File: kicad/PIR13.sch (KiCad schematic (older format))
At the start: 22 parts, among them P301 PIR13, Q301 IRLML2502, Q302 IRLML2502, Q303 IRLML2502

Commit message: Started assigning foot prints to the parts
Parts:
- C301, C302, C303: footprint (none) -> Capacitors_SMD:C_0805
- D301, D302, D303: footprint (none) -> LEDs:LED_0805
- P301: footprint (none) -> Pin_Headers:Pin_Header_Straight_1x09; Conrad-PN (none) -> Value; Digikey-PN (none) -> Value; MFP (none) -> Value
- Q301, Q302, Q303: footprint Micro3 -> TO_SOT_Packages_SMD:SOT-23; Conrad-PN (none) -> 162827 - 62; Digikey-PN (none) -> IRLML2502GTRPBFCT-ND; MFP TPS70933DBVR -> IRLML2502GTRPBF
- R301, R302, R303: footprint (none) -> Resistors_SMD:R_0805
- R304: renamed from R307; footprint (none) -> Resistors_SMD:R_0805
- R305: renamed from R308; footprint (none) -> Resistors_SMD:R_0805
- R306: renamed from R309; footprint (none) -> Resistors_SMD:R_0805
- R307: renamed from R304; footprint (none) -> Resistors_SMD:R_0805
- R308: renamed from R305; footprint (none) -> Resistors_SMD:R_0805
- R309: renamed from R306; footprint (none) -> Resistors_SMD:R_0805
- TP301, TP302: footprint (none) -> Measurement_Points:Measurement_Point_Round-SMD-Pad_Small
- TP303: renamed from TP?; footprint (none) -> Measurement_Points:Measurement_Point_Round-SMD-Pad_Small

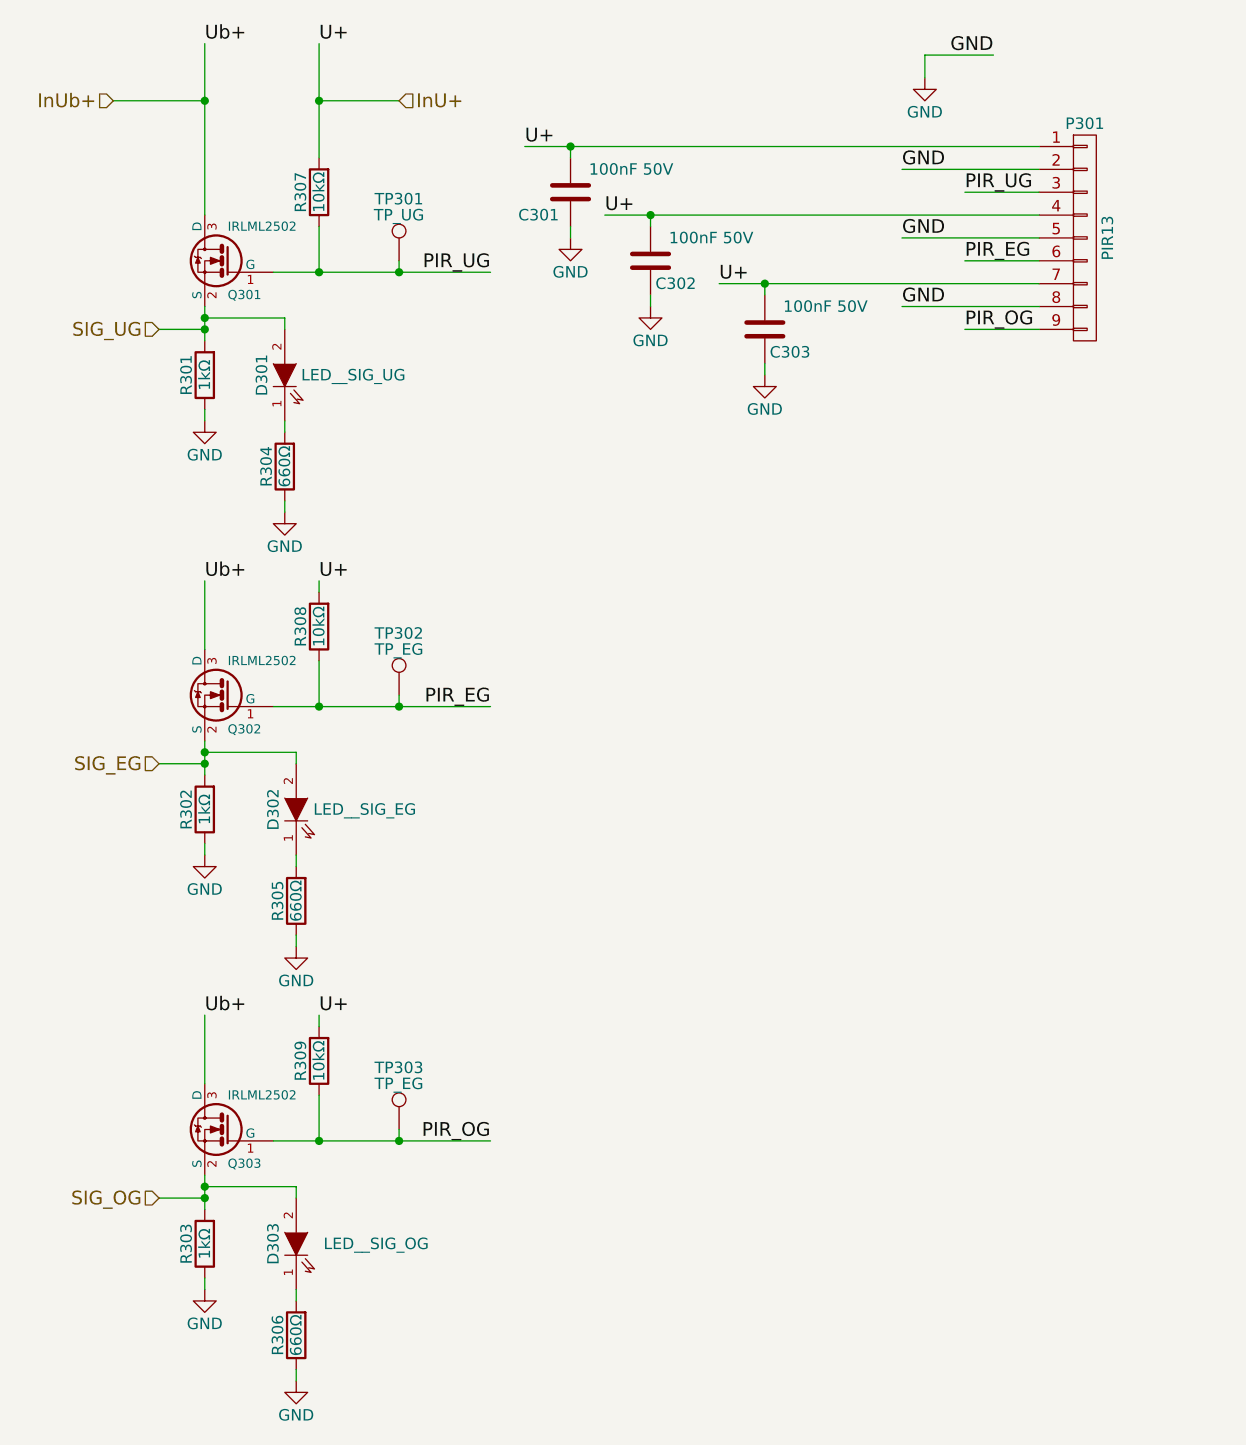
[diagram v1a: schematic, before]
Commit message: Started adding tracks to the layout
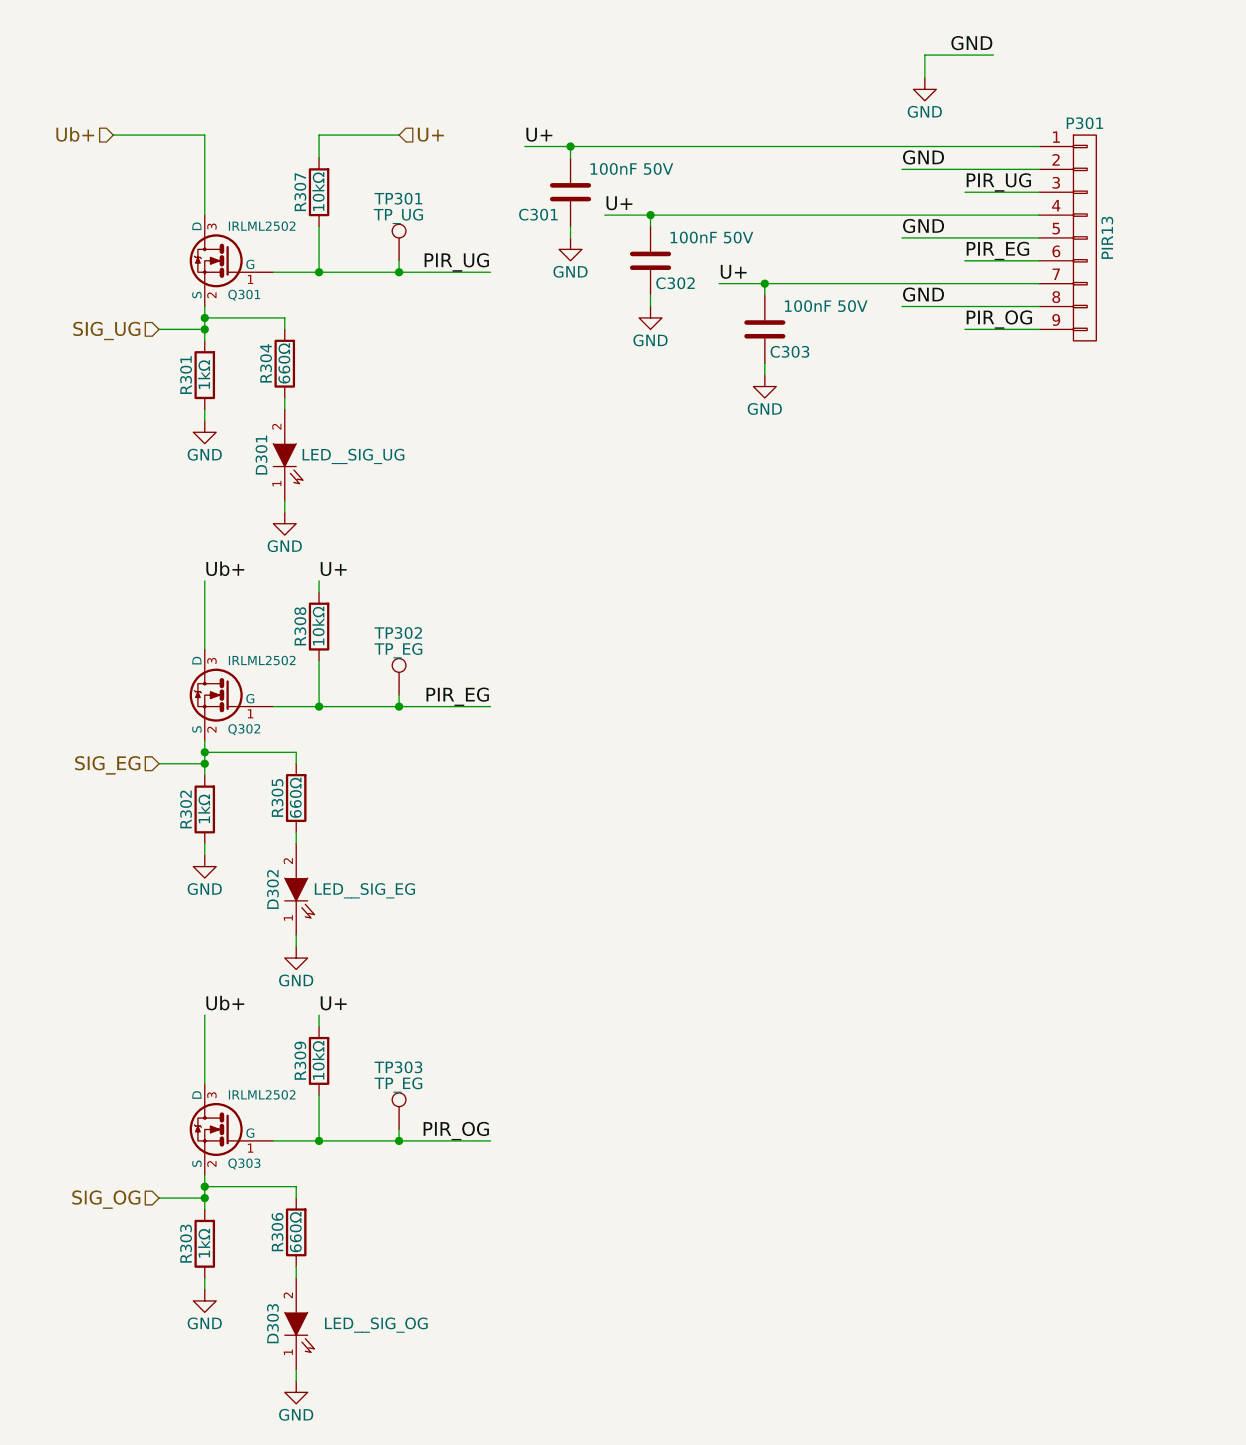
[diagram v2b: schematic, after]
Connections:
- net GND: now also D301.1 (K), D302.1 (K), D303.1 (K); no longer R304.1, R305.1, R306.1
- net SIG_EG: now also R305.2; no longer D302.2 (A)
- net SIG_OG: now also R306.2; no longer D303.2 (A)
- net SIG_UG: now also R304.2; no longer D301.2 (A)
- net InU+ renamed U+
- net InUb+ renamed Ub+
- new net: D301.2 (A), R304.1
- new net: D302.2 (A), R305.1
- new net: D303.2 (A), R306.1
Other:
- moved on the sheet: D301, D302, D303, R304, R305, R306
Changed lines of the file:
@@
 PIR_OG
 $Comp
-L GND #PWR015
+L GND #PWR018
 U 1 1 585206AF
 P 5550 1150
-F 0 "#PWR015" H 5550 900 50  0001 C CNN
+F 0 "#PWR018" H 5550 900 50  0001 C CNN
 F 1 "GND" H 5550 1000 50  0000 C CNN
 F 2 "" H 5550 1150 50  0000 C CNN
@@
 	-1   0    0    1
 $EndComp
-Text HLabel 3250 1250 2    60   Input ~ 0
-InU+
+Text HLabel 3250 1400 2    60   Input ~ 0
+U+
 Text Label 5450 1550 0    60   ~ 0
 GND
@@
 	-1   0    0    -1
 $EndComp
-Text Label 2400 1000 0    60   ~ 0
-Ub+
 $Comp
 L R R301
@@
 	-1   0    0    1
 $EndComp
-Text Label 2900 1000 0    60   ~ 0
-U+
 Text Label 3650 2000 2    60   ~ 0
 PIR_UG
-Text HLabel 2000 1250 0    60   Input ~ 0
-InUb+
-$Comp
-L GND #PWR016
+Text HLabel 2000 1400 0    60   Input ~ 0
+Ub+
+$Comp
+L GND #PWR019
 U 1 1 585215A4
 P 2400 2650
-F 0 "#PWR016" H 2400 2400 50  0001 C CNN
+F 0 "#PWR019" H 2400 2400 50  0001 C CNN
 F 1 "GND" H 2400 2500 50  0000 C CNN
 F 2 "" H 2400 2650 50  0000 C CNN
@@
 PIR_EG
 $Comp
-L GND #PWR017
+L GND #PWR020
 U 1 1 58521B24
 P 2400 4550
-F 0 "#PWR017" H 2400 4300 50  0001 C CNN
+F 0 "#PWR020" H 2400 4300 50  0001 C CNN
 F 1 "GND" H 2400 4400 50  0000 C CNN
 F 2 "" H 2400 4550 50  0000 C CNN
@@
 PIR_OG
 $Comp
-L GND #PWR018
+L GND #PWR021
 U 1 1 58521C75
 P 2400 6450
-F 0 "#PWR018" H 2400 6200 50  0001 C CNN
+F 0 "#PWR021" H 2400 6200 50  0001 C CNN
 F 1 "GND" H 2400 6300 50  0000 C CNN
 F 2 "" H 2400 6450 50  0000 C CNN
@@
 L LED D301
 U 1 1 5852C267
-P 2750 2450
-F 0 "D301" H 2750 2550 50  0000 C CNN
-F 1 "LED__SIG_UG" V 2750 2150 50  0000 C CNN
-F 2 "LEDs:LED_0805" H 2750 2450 50  0001 C CNN
-F 3 "" H 2750 2450 50  0000 C CNN
-	1    2750 2450
+P 2750 2800
+F 0 "D301" H 2750 2900 50  0000 C CNN
+F 1 "LED__SIG_UG" V 2750 2500 50  0000 C CNN
+F 2 "LEDs:LED_0805" H 2750 2800 50  0001 C CNN
+F 3 "" H 2750 2800 50  0000 C CNN
+	1    2750 2800
 	0    -1   -1   0
 $EndComp
@@
 L R R304
 U 1 1 5852C57E
-P 2750 2850
-F 0 "R304" V 2830 2850 50  0000 C CNN
-F 1 "660Ω" V 2750 2850 50  0000 C CNN
-F 2 "Resistors_SMD:R_0805" V 2680 2850 50  0001 C CNN
-F 3 "" H 2750 2850 50  0000 C CNN
-	1    2750 2850
+P 2750 2400
+F 0 "R304" V 2830 2400 50  0000 C CNN
+F 1 "660Ω" V 2750 2400 50  0000 C CNN
+F 2 "Resistors_SMD:R_0805" V 2680 2400 50  0001 C CNN
+F 3 "" H 2750 2400 50  0000 C CNN
+	1    2750 2400
 	-1   0    0    1
 $EndComp
@@
 L LED D302
 U 1 1 5852CAA2
-P 2800 4350
-F 0 "D302" H 2800 4450 50  0000 C CNN
-F 1 "LED__SIG_EG" V 2800 4050 50  0000 C CNN
-F 2 "LEDs:LED_0805" H 2800 4350 50  0001 C CNN
-F 3 "" H 2800 4350 50  0000 C CNN
-	1    2800 4350
+P 2800 4700
+F 0 "D302" H 2800 4800 50  0000 C CNN
+F 1 "LED__SIG_EG" V 2800 4400 50  0000 C CNN
+F 2 "LEDs:LED_0805" H 2800 4700 50  0001 C CNN
+F 3 "" H 2800 4700 50  0000 C CNN
+	1    2800 4700
 	0    -1   -1   0
 $EndComp
@@
 L R R305
 U 1 1 5852CAA8
-P 2800 4750
-F 0 "R305" V 2880 4750 50  0000 C CNN
-F 1 "660Ω" V 2800 4750 50  0000 C CNN
-F 2 "Resistors_SMD:R_0805" V 2730 4750 50  0001 C CNN
-F 3 "" H 2800 4750 50  0000 C CNN
-	1    2800 4750
-	-1   0    0    1
-$EndComp
-$Comp
-L GND #PWR019
+P 2800 4300
+F 0 "R305" V 2880 4300 50  0000 C CNN
+F 1 "660Ω" V 2800 4300 50  0000 C CNN
+F 2 "Resistors_SMD:R_0805" V 2730 4300 50  0001 C CNN
+F 3 "" H 2800 4300 50  0000 C CNN
+	1    2800 4300
+	-1   0    0    1
+$EndComp
+$Comp
+L GND #PWR022
 U 1 1 5852CAAF
 P 2800 4950
-F 0 "#PWR019" H 2800 4700 50  0001 C CNN
+F 0 "#PWR022" H 2800 4700 50  0001 C CNN
 F 1 "GND" H 2800 4800 50  0000 C CNN
 F 2 "" H 2800 4950 50  0000 C CNN
@@
 L LED D303
 U 1 1 5852D26A
-P 2800 6250
-F 0 "D303" H 2800 6350 50  0000 C CNN
-F 1 "LED__SIG_OG" V 2800 5900 50  0000 C CNN
-F 2 "LEDs:LED_0805" H 2800 6250 50  0001 C CNN
-F 3 "" H 2800 6250 50  0000 C CNN
-	1    2800 6250
+P 2800 6600
+F 0 "D303" H 2800 6700 50  0000 C CNN
+F 1 "LED__SIG_OG" V 2800 6250 50  0000 C CNN
+F 2 "LEDs:LED_0805" H 2800 6600 50  0001 C CNN
+F 3 "" H 2800 6600 50  0000 C CNN
+	1    2800 6600
 	0    -1   -1   0
 $EndComp
@@
 L R R306
 U 1 1 5852D270
-P 2800 6650
-F 0 "R306" V 2880 6650 50  0000 C CNN
-F 1 "660Ω" V 2800 6650 50  0000 C CNN
-F 2 "Resistors_SMD:R_0805" V 2730 6650 50  0001 C CNN
-F 3 "" H 2800 6650 50  0000 C CNN
-	1    2800 6650
-	-1   0    0    1
-$EndComp
-$Comp
-L GND #PWR020
+P 2800 6200
+F 0 "R306" V 2880 6200 50  0000 C CNN
+F 1 "660Ω" V 2800 6200 50  0000 C CNN
+F 2 "Resistors_SMD:R_0805" V 2730 6200 50  0001 C CNN
+F 3 "" H 2800 6200 50  0000 C CNN
+	1    2800 6200
+	-1   0    0    1
+$EndComp
+$Comp
+L GND #PWR023
 U 1 1 5852D277
 P 2800 6850
-F 0 "#PWR020" H 2800 6600 50  0001 C CNN
+F 0 "#PWR023" H 2800 6600 50  0001 C CNN
 F 1 "GND" H 2800 6700 50  0000 C CNN
 F 2 "" H 2800 6850 50  0000 C CNN
@@
 $EndComp
 $Comp
-L GND #PWR021
+L GND #PWR024
 U 1 1 5852E037
 P 4000 1850
-F 0 "#PWR021" H 4000 1600 50  0001 C CNN
+F 0 "#PWR024" H 4000 1600 50  0001 C CNN
 F 1 "GND" H 4000 1700 50  0000 C CNN
 F 2 "" H 4000 1850 50  0000 C CNN
@@
 $EndComp
 $Comp
-L GND #PWR022
+L GND #PWR025
 U 1 1 5852E38D
 P 4350 2150
-F 0 "#PWR022" H 4350 1900 50  0001 C CNN
+F 0 "#PWR025" H 4350 1900 50  0001 C CNN
 F 1 "GND" H 4350 2000 50  0000 C CNN
 F 2 "" H 4350 2150 50  0000 C CNN
@@
 $EndComp
 $Comp
-L GND #PWR023
+L GND #PWR026
 U 1 1 5852E6E2
 P 4850 2450
-F 0 "#PWR023" H 4850 2200 50  0001 C CNN
+F 0 "#PWR026" H 4850 2200 50  0001 C CNN
 F 1 "GND" H 4850 2300 50  0000 C CNN
 F 2 "" H 4850 2450 50  0000 C CNN
@@
 Connection ~ 2900 2000
 Wire Wire Line
-	2400 1000 2400 1750
-Wire Wire Line
 	2400 2600 2400 2650
 Wire Wire Line
-	2900 1000 2900 1500
-Wire Wire Line
-	2000 1250 2400 1250
-Connection ~ 2400 1250
+	2000 1400 2400 1400
 Wire Wire Line
 	2400 2250 2200 2250
@@
 Connection ~ 2400 6050
 Wire Wire Line
-	2750 2650 2750 2700
-Wire Wire Line
 	2750 3000 2750 3050
-Wire Wire Line
-	2800 4550 2800 4600
 Wire Wire Line
 	2800 4900 2800 4950
@@
 Connection ~ 2400 4100
 Wire Wire Line
-	2800 6450 2800 6500
-Wire Wire Line
 	2800 6800 2800 6850
 Wire Wire Line
@@
 	4850 2400 4850 2450
 Wire Wire Line
-	3250 1250 2900 1250
-Connection ~ 2900 1250
+	3250 1400 2900 1400
 Wire Wire Line
 	4850 2050 4850 2100
@@
 Connection ~ 2400 2200
 $Comp
-L GND #PWR024
+L GND #PWR027
 U 1 1 5852C6FF
 P 2750 3050
-F 0 "#PWR024" H 2750 2800 50  0001 C CNN
+F 0 "#PWR027" H 2750 2800 50  0001 C CNN
 F 1 "GND" H 2750 2900 50  0000 C CNN
 F 2 "" H 2750 3050 50  0000 C CNN
@@
 	1    0    0    -1
 $EndComp
+Wire Wire Line
+	2400 1400 2400 1750
+Wire Wire Line
+	2900 1400 2900 1500
+Wire Wire Line
+	2750 2550 2750 2600
+Wire Wire Line
+	2800 4450 2800 4500
+Wire Wire Line
+	2800 6350 2800 6400
 $EndSCHEMATC

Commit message: Revamped the master pcb layout for the mounting holes and the actual footprint for the terminal blocks
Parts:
- P301: footprint Pin_Headers:Pin_Header_Straight_1x09 -> tl2c-footprint:Spring_Terminal_Block_1_x_9; Reichelt-PN (none) -> AST 041
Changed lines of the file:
@@
 F 0 "P301" H 6250 2350 50  0000 C CNN
 F 1 "PIR13" V 6350 1850 50  0000 C CNN
-F 2 "Pin_Headers:Pin_Header_Straight_1x09" H 6250 1850 50  0001 C CNN
+F 2 "tl2c-footprint:Spring_Terminal_Block_1_x_9" H 6250 1850 50  0001 C CNN
 F 3 "" H 6250 1850 50  0000 C CNN
 F 4 "Value" H 6250 1850 60  0001 C CNN "MFP"
 F 5 "Value" H 6250 1850 60  0001 C CNN "Conrad-PN"
 F 6 "Value" H 6250 1850 60  0001 C CNN "Digikey-PN"
+F 7 "AST 041" H 6250 1850 60  0001 C CNN "Reichelt-PN"
 	1    6250 1850
 	1    0    0    -1

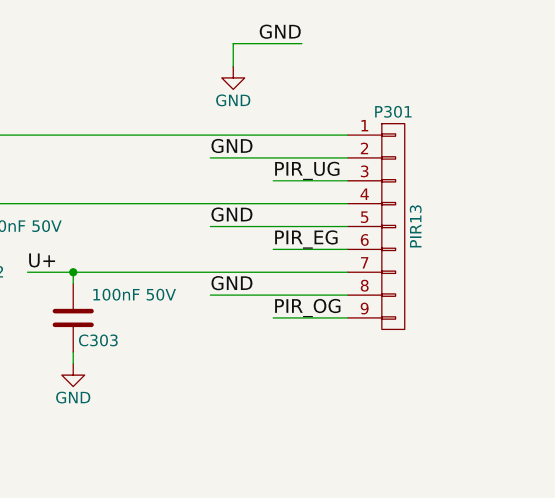
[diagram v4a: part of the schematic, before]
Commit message: Finished off the refactoring for the housing and terminal blocks
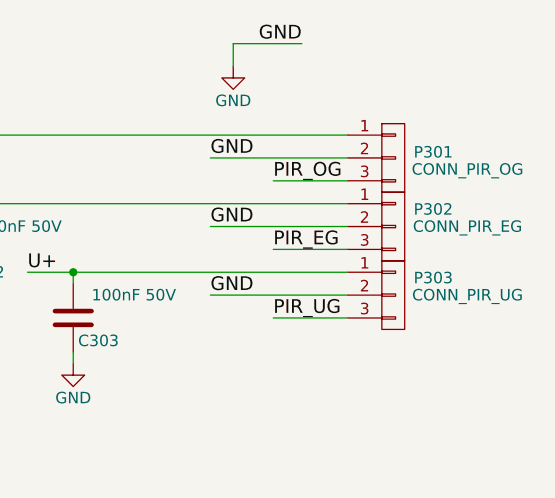
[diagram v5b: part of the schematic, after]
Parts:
- removed P301: PIR13, tl2c-footprint:Spring_Terminal_Block_1_x_9, symbol CONN_01X09
- added P301: CONN_PIR_OG, tl2c-footprint:Spring_Terminal_Block_1_x_3, symbol CONN_01X03
- added P302: CONN_PIR_EG, tl2c-footprint:Spring_Terminal_Block_1_x_3, symbol CONN_01X03
- added P303: CONN_PIR_UG, tl2c-footprint:Spring_Terminal_Block_1_x_3, symbol CONN_01X03
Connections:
- net GND: now also P301.2 (P2), P302.2 (P2), P303.2 (P2)
- net PIR_EG: now also P302.3 (P3)
- net PIR_OG: now also P301.3 (P3)
- net PIR_UG: now also P303.3 (P3)
- net U+: now also P301.1 (P1), P302.1 (P1), P303.1 (P1)
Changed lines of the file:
@@
 Comment4 ""
 $EndDescr
-$Comp
-L CONN_01X09 P301
-U 1 1 585206A2
-P 6250 1850
-F 0 "P301" H 6250 2350 50  0000 C CNN
-F 1 "PIR13" V 6350 1850 50  0000 C CNN
-F 2 "tl2c-footprint:Spring_Terminal_Block_1_x_9" H 6250 1850 50  0001 C CNN
-F 3 "" H 6250 1850 50  0000 C CNN
-F 4 "Value" H 6250 1850 60  0001 C CNN "MFP"
-F 5 "Value" H 6250 1850 60  0001 C CNN "Conrad-PN"
-F 6 "Value" H 6250 1850 60  0001 C CNN "Digikey-PN"
-F 7 "AST 041" H 6250 1850 60  0001 C CNN "Reichelt-PN"
-	1    6250 1850
-	1    0    0    -1
-$EndComp
-Text Label 5725 1650 0    60   ~ 0
+Text Label 5725 2250 0    60   ~ 0
 PIR_UG
 Text Label 5725 1950 0    60   ~ 0
 PIR_EG
-Text Label 5725 2250 0    60   ~ 0
+Text Label 5725 1650 0    60   ~ 0
 PIR_OG
 $Comp
@@
 Wire Wire Line
 	2800 6350 2800 6400
+$Comp
+L CONN_01X03 P301
+U 1 1 5867BA07
+P 6250 1550
+F 0 "P301" H 6425 1575 50  0000 C CNN
+F 1 "CONN_PIR_OG" H 6575 1500 50  0000 C CNN
+F 2 "tl2c-footprint:Spring_Terminal_Block_1_x_3" H 6250 1550 50  0001 C CNN
+F 3 "" H 6250 1550 50  0000 C CNN
+F 4 "Value" H 6250 1550 60  0001 C CNN "MFP"
+F 5 "Value" H 6250 1550 60  0001 C CNN "Conrad-PN"
+F 6 "Value" H 6250 1550 60  0001 C CNN "Digikey-PN"
+	1    6250 1550
+	1    0    0    -1
+$EndComp
+$Comp
+L CONN_01X03 P302
+U 1 1 5867BAEB
+P 6250 1850
+F 0 "P302" H 6425 1925 50  0000 C CNN
+F 1 "CONN_PIR_EG" H 6575 1850 50  0000 C CNN
+F 2 "tl2c-footprint:Spring_Terminal_Block_1_x_3" H 6250 1850 50  0001 C CNN
+F 3 "" H 6250 1850 50  0000 C CNN
+F 4 "Value" H 6250 1850 60  0001 C CNN "MFP"
+F 5 "Value" H 6250 1850 60  0001 C CNN "Conrad-PN"
+F 6 "Value" H 6250 1850 60  0001 C CNN "Digikey-PN"
+	1    6250 1850
+	1    0    0    -1
+$EndComp
+$Comp
+L CONN_01X03 P303
+U 1 1 5867BB77
+P 6250 2150
+F 0 "P303" H 6425 2225 50  0000 C CNN
+F 1 "CONN_PIR_UG" H 6575 2150 50  0000 C CNN
+F 2 "tl2c-footprint:Spring_Terminal_Block_1_x_3" H 6250 2150 50  0001 C CNN
+F 3 "" H 6250 2150 50  0000 C CNN
+F 4 "Value" H 6250 2150 60  0001 C CNN "MFP"
+F 5 "Value" H 6250 2150 60  0001 C CNN "Conrad-PN"
+F 6 "Value" H 6250 2150 60  0001 C CNN "Digikey-PN"
+	1    6250 2150
+	1    0    0    -1
+$EndComp
 $EndSCHEMATC
